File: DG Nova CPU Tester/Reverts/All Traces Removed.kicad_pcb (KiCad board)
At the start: 2 copper layers, 414.8 x 131.4 mm, 115 parts, among them J1 Front Panel Socket - Backside, J10 Programmed I/O, J11 CPU Option Inputs, J12 Data Channel, J13 Program Interrupt, J14 System Control, J15 Slot_02x50_Odd_Even, J16 Slot_02x50_Odd_Even, J17 CPU Option Outputs, J18 MEM Control Outputs, J19 Logic 8 CH, J20 Logic 8 CH, J21 Arduino Anolog Pins, J22 Arduino Digital Pins, J23 Arduino Digital Pins, J4 ATX-24, J5 Front Panel Card Edge, J6 MBO, J7 MEM, J8 Data Channel, J9 Front Panel Controls, SW1 SW_Push, U1 74HC14, U2 Pico

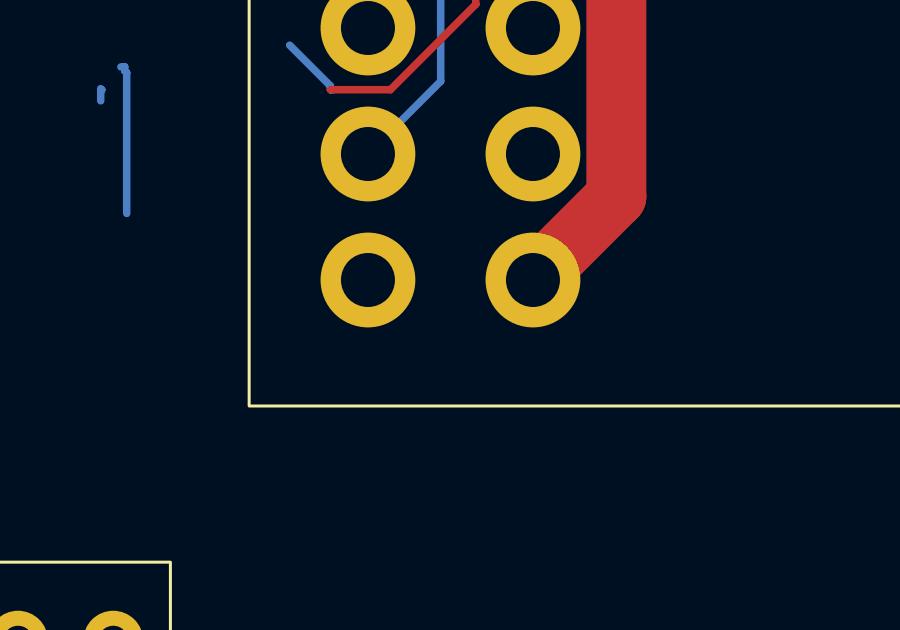
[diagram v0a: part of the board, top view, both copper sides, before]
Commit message: All Traces Removed
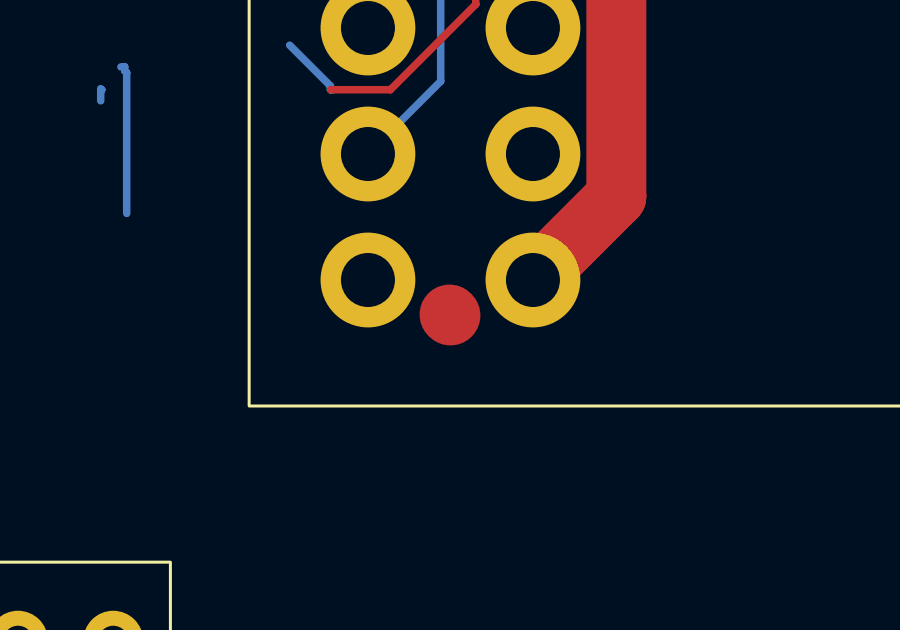
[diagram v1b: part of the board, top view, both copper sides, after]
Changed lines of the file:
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@@
   (segment locked (start 546.18 40.56) (end 562.356 40.56) (width 0.25) (layer "B.Cu") (net 6))
   (segment locked (start 566.783 42.436) (end 566.783 42.436001) (width 0.25) (layer "F.Cu") (net 7))
+  (segment (start 425.26 111.791514) (end 425.23 111.761514) (width 2) (layer "F.Cu") (net 7))
   (segment locked (start 566.783 42.436001) (end 566.91 42.563001) (width 0.25) (layer "F.Cu") (net 7))
   (segment locked (start 565.658 32.893) (end 566.783 34.018) (width 0.25) (layer "F.Cu") (net 7))
